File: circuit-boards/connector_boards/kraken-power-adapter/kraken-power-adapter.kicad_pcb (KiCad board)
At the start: 2 copper layers, 41.6 x 33.4 mm, 5 parts, among them J1 Vbat+, J2 Vbat-, J3 Vbat PP15-45

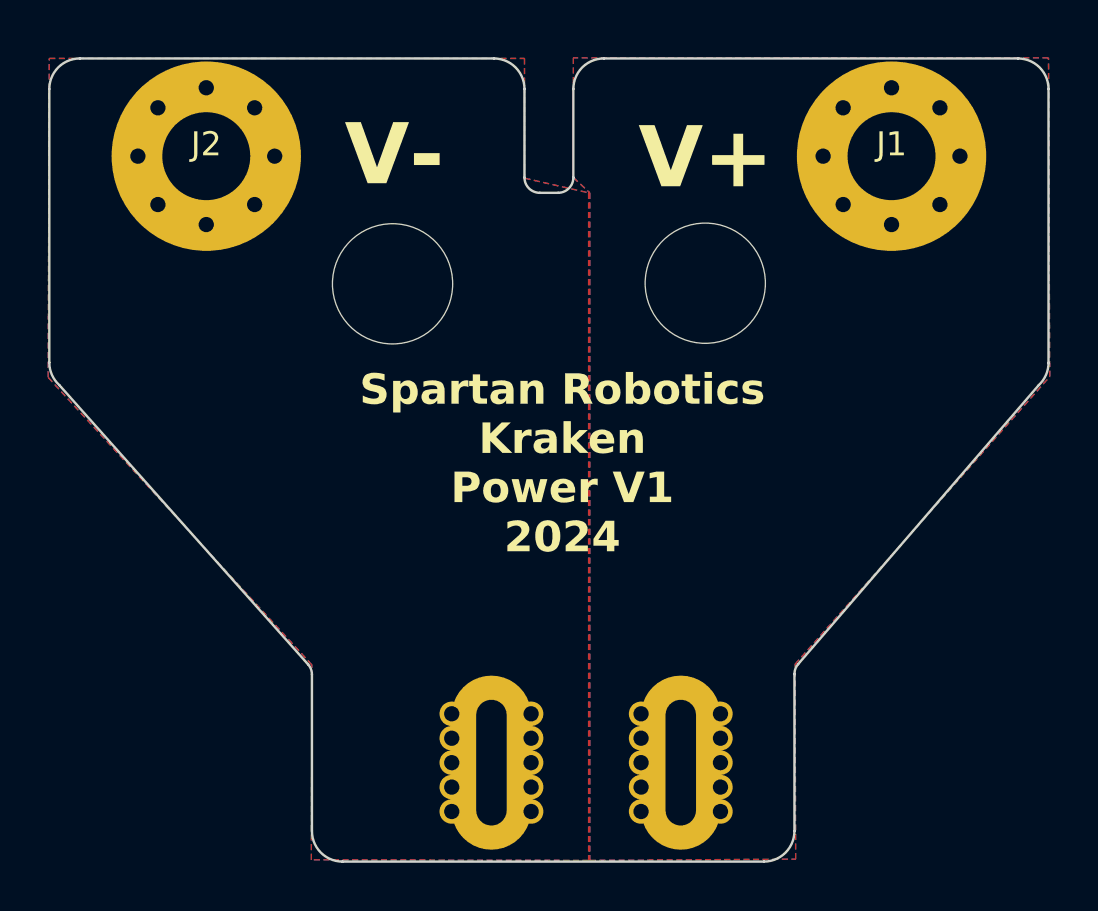
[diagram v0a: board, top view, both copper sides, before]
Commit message: Modified kraken power to rotate andersons 90 deg
Signed-off-by: Scott Berman <sgberman1@gmail.com>
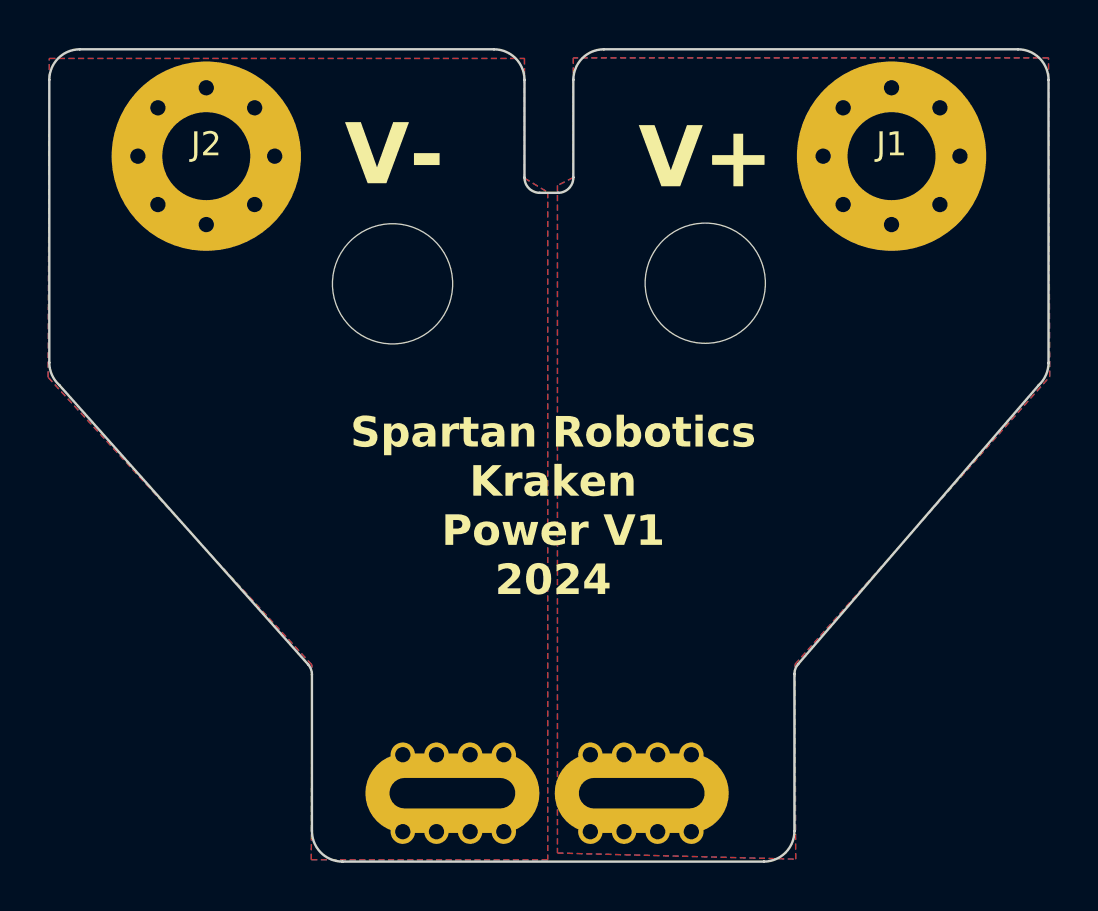
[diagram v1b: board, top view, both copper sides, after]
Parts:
- J3: footprint kraken-adapter:Dual-stacked-1335G1 -> kraken-adapter:Dual-side-by-side-1335G1
- moved J3 1.30 mm to (106.2, 131.6), turned to 0 degrees
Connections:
- J3 pad 1: /Vbat+ -> /Vbat-
- J3 pad 2: /Vbat- -> /Vbat+
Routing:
- added copper zone on In1.Cu, net /Vbat+
- added copper zone on In2.Cu, net /Vbat+
- added copper zone on In1.Cu, net /Vbat-
- added copper zone on In2.Cu, net /Vbat-
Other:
- board size 41.6 x 33.4 mm -> 41.6 x 33.8 mm
- copper layers 2 -> 4
- board text added: "1636.00 mils x 1330.00 mils"
- board text added: "3.937007874 mils"
- board text added: "4"
- board text added: "40.13858268 mils"
- board text added: "60.00 mils"
- board text added: "In1.Cu"
- board text added: "In2.Cu"
- board text added: "prepreg"
- board text removed: "1636.00 mils x 1315.00 mils"
- board text removed: "2"
- board text removed: "59.4488189 mils"
- board text removed: "65.84 mils"
